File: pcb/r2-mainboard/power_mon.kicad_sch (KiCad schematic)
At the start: 29 parts, among them U1200 INA3221, U1201 INA3221, U1202 INA3221

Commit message: routing
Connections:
- net +3V3_AON: now also R1213.2, R1215.2
- net +3V3_DCDC: no longer R1213.2, R1215.2
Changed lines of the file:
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@@
 			)
 		)
-		(property "Value" "+3V3_DCDC"
+		(property "Value" "+3V3_AON"
 			(at 240.03 93.9799 90)
 			(show_name no)
@@
 			)
 		)
-		(property "Value" "+3V3_DCDC"
+		(property "Value" "+3V3_AON"
 			(at 240.03 78.7399 90)
 			(show_name no)

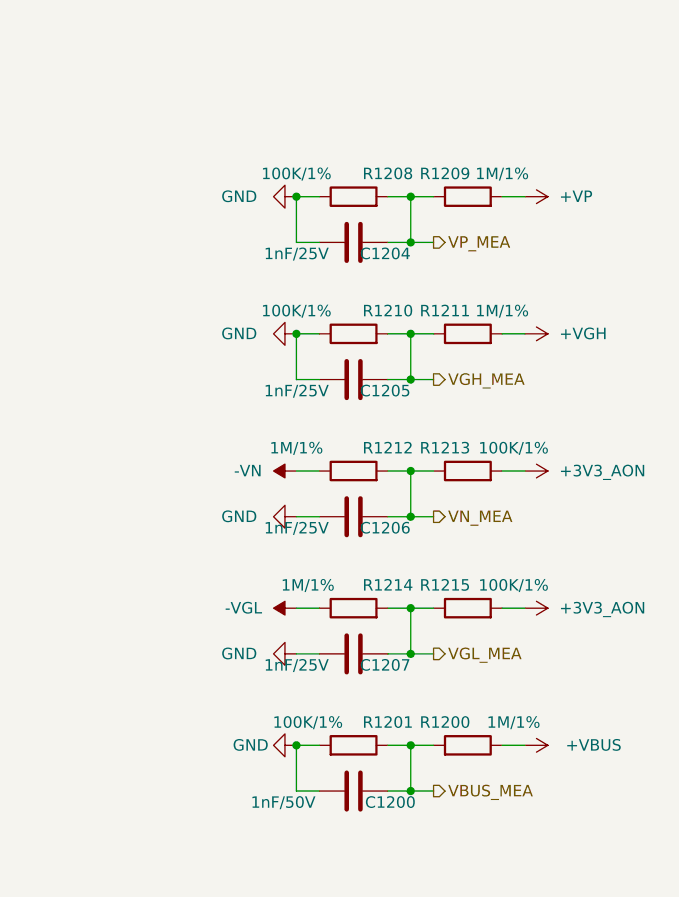
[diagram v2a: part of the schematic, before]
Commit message: Schematics update for new chip.
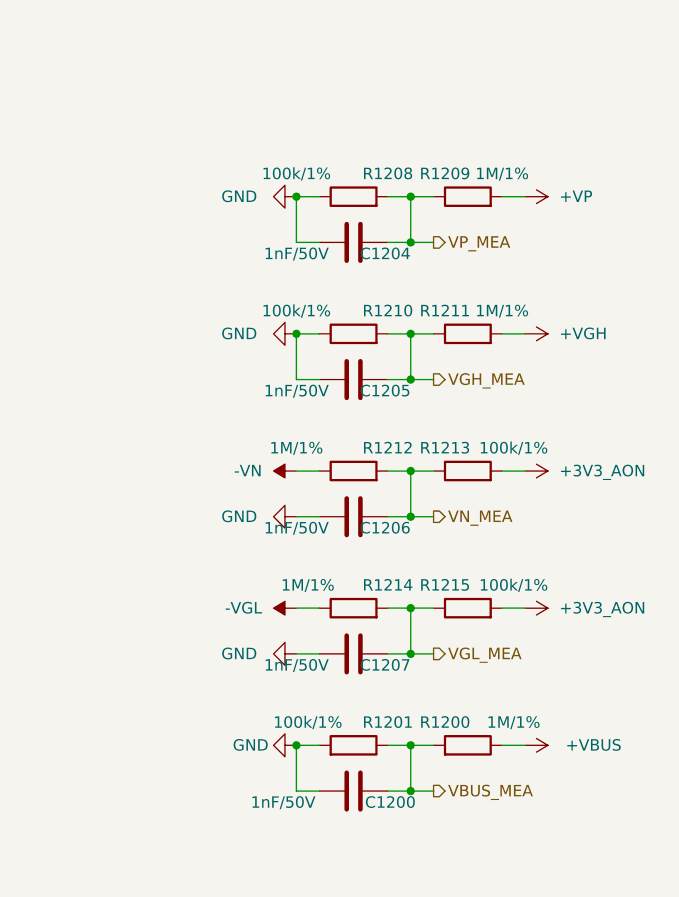
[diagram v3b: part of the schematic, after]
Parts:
- C1204, C1205, C1206, C1207: value 1nF/25V -> 1nF/50V
- R1201, R1208, R1210, R1213, R1215: value 100K/1% -> 100k/1%
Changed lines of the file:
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@@
 			)
 		)
-		(property "Value" "100K/1%"
+		(property "Value" "100k/1%"
 			(at 234.95 76.2 90)
 			(show_name no)
@@
 			)
 		)
-		(property "Value" "1nF/25V"
+		(property "Value" "1nF/50V"
 			(at 210.82 69.85 90)
 			(show_name no)
@@
 			)
 		)
-		(property "Value" "1nF/25V"
+		(property "Value" "1nF/50V"
 			(at 210.82 54.61 90)
 			(show_name no)
@@
 			)
 		)
-		(property "Value" "100K/1%"
+		(property "Value" "100k/1%"
 			(at 210.82 45.72 90)
 			(show_name no)
@@
 			)
 		)
-		(property "Value" "1nF/25V"
+		(property "Value" "1nF/50V"
 			(at 210.82 85.09 90)
 			(show_name no)
@@
 			)
 		)
-		(property "Value" "100K/1%"
+		(property "Value" "100k/1%"
 			(at 234.95 91.44 90)
 			(show_name no)
@@
 			)
 		)
-		(property "Value" "100K/1%"
+		(property "Value" "100k/1%"
 			(at 212.09 106.68 90)
 			(show_name no)
@@
 			)
 		)
-		(property "Value" "1nF/25V"
+		(property "Value" "1nF/50V"
 			(at 210.82 100.33 90)
 			(show_name no)
@@
 			)
 		)
-		(property "Value" "100K/1%"
+		(property "Value" "100k/1%"
 			(at 210.82 60.96 90)
 			(show_name no)
